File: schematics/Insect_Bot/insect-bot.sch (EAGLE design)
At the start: 26 parts, among them Q1 2N2222, U1 L4931-TO92-AMMO, U2 ARDUINO_MINI

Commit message: First completed insect bot PCB.
First revision with poured-copper ground plane.
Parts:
- added JP4, JP5: STAND-OFF, SparkFun-Electromechanical:STAND-OFF
- S2: value TILTSWITCH -> tilt
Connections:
- net GND: now also S2.1; no longer S2.2
- net N$1: now also S1.S
- net N$12: now also S2.2; no longer S2.1
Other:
- moved on the sheet: S2
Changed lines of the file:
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@@
 </variantdefs>
 <classes>
-<class number="0" name="default" width="0" drill="0">
+<class number="0" name="default" width="0.3048" drill="0.2032">
+<clearance class="0" value="0.2032"/>
+</class>
+<class number="1" name="power" width="0.4064" drill="0.2032">
+<clearance class="1" value="0.2032"/>
 </class>
 </classes>
@@
 <part name="P+7" library="SparkFun-Aesthetics" deviceset="VCC" device=""/>
 <part name="GND10" library="SparkFun-Aesthetics" deviceset="GND" device=""/>
-<part name="S2" library="jb-eagle" deviceset="TILTSWITCH" device=""/>
 <part name="GND11" library="SparkFun-Aesthetics" deviceset="GND" device=""/>
 <part name="R9" library="SparkFun-Passives" deviceset="RESISTOR" device="AXIAL-0.3" value="330"/>
 <part name="LED2" library="SparkFun-LED" deviceset="LED" device="3MM" value="red"/>
 <part name="GND12" library="SparkFun-Aesthetics" deviceset="GND" device=""/>
+<part name="S2" library="jb-eagle" deviceset="TILTSWITCH" device="" value="tilt"/>
+<part name="JP4" library="SparkFun-Electromechanical" deviceset="STAND-OFF" device=""/>
+<part name="JP5" library="SparkFun-Electromechanical" deviceset="STAND-OFF" device=""/>
 </parts>
 <sheets>
@@
 <instance part="P+7" gate="1" x="177.8" y="119.38"/>
 <instance part="GND10" gate="1" x="177.8" y="81.28"/>
-<instance part="S2" gate="G$1" x="152.4" y="81.28" rot="R270"/>
 <instance part="GND11" gate="1" x="152.4" y="71.12"/>
 <instance part="R9" gate="G$1" x="139.7" y="81.28" rot="R90"/>
 <instance part="LED2" gate="G$1" x="139.7" y="71.12"/>
 <instance part="GND12" gate="1" x="139.7" y="60.96"/>
+<instance part="S2" gate="G$1" x="152.4" y="81.28" rot="R90"/>
+<instance part="JP4" gate="G$1" x="104.14" y="-5.08"/>
+<instance part="JP5" gate="G$1" x="109.22" y="-5.08"/>
 </instances>
 <busses>
 </busses>
 <nets>
-<net name="GND" class="0">
+<net name="GND" class="1">
 <segment>
 <pinref part="JP1" gate="G$1" pin="2"/>
@@
 </segment>
 <segment>
-<pinref part="S2" gate="G$1" pin="2"/>
 <pinref part="GND11" gate="1" pin="GND"/>
 <wire x1="152.4" y1="76.2" x2="152.4" y2="73.66" width="0.1524" layer="91"/>
+<pinref part="S2" gate="G$1" pin="1"/>
 </segment>
 <segment>
@@
 </segment>
 </net>
-<net name="N$1" class="0">
+<net name="N$1" class="1">
 <segment>
 <pinref part="JP1" gate="G$1" pin="1"/>
 <pinref part="S1" gate="1" pin="P"/>
 <wire x1="-5.08" y1="22.86" x2="2.54" y2="22.86" width="0.1524" layer="91"/>
-</segment>
-</net>
-<net name="N$2" class="0">
+<pinref part="S1" gate="1" pin="S"/>
+<wire x1="10.16" y1="20.32" x2="10.16" y2="17.78" width="0.1524" layer="91"/>
+<wire x1="10.16" y1="17.78" x2="2.54" y2="17.78" width="0.1524" layer="91"/>
+<wire x1="2.54" y1="17.78" x2="2.54" y2="22.86" width="0.1524" layer="91"/>
+<junction x="2.54" y="22.86"/>
+</segment>
+</net>
+<net name="N$2" class="1">
 <segment>
 <pinref part="S1" gate="1" pin="O"/>
@@
 </segment>
 </net>
-<net name="V_IN" class="0">
+<net name="V_IN" class="1">
 <segment>
 <pinref part="D1" gate="G$1" pin="C"/>
@@
 <segment>
 <pinref part="U2" gate="G$1" pin="A0"/>
-<pinref part="S2" gate="G$1" pin="1"/>
 <wire x1="114.3" y1="88.9" x2="152.4" y2="88.9" width="0.1524" layer="91"/>
 <wire x1="152.4" y1="88.9" x2="152.4" y2="86.36" width="0.1524" layer="91"/>
-</segment>
-</net>
+<pinref part="S2" gate="G$1" pin="2"/>
+</segment>
+</net>

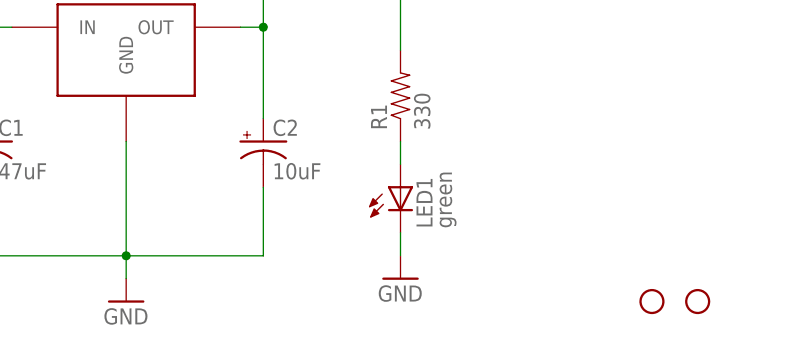
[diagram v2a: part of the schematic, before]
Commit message: Final layout for insect bot board.
Made traces a bit wider. Increased size of pad for the IR remote
receiver.
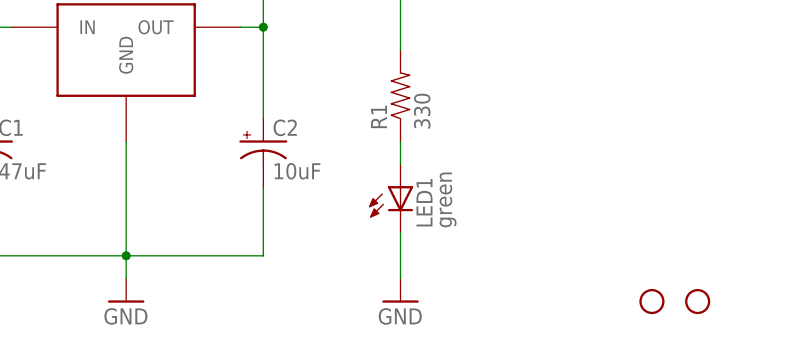
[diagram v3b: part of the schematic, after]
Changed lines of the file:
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@@
 <part name="P+6" library="SparkFun-Aesthetics" deviceset="VCC" device=""/>
 <part name="GND8" library="SparkFun-Aesthetics" deviceset="GND" device=""/>
-<part name="IRM1" library="jb-eagle" deviceset="AX-1838" device=""/>
 <part name="R6" library="SparkFun-Passives" deviceset="RESISTOR" device="AXIAL-0.3" value="47"/>
 <part name="R7" library="SparkFun-Passives" deviceset="RESISTOR" device="AXIAL-0.3" value="10k"/>
@@
 <part name="JP4" library="SparkFun-Electromechanical" deviceset="STAND-OFF" device=""/>
 <part name="JP5" library="SparkFun-Electromechanical" deviceset="STAND-OFF" device=""/>
+<part name="IRM1" library="jb-eagle" deviceset="AX-1838" device=""/>
 </parts>
 <sheets>
@@
 <instance part="GND5" gate="1" x="139.7" y="99.06"/>
 <instance part="GND6" gate="1" x="154.94" y="96.52"/>
-<instance part="GND7" gate="1" x="76.2" y="-2.54"/>
+<instance part="GND7" gate="1" x="76.2" y="-5.08"/>
 <instance part="P+5" gate="1" x="60.96" y="33.02"/>
 <instance part="JP3" gate="G$1" x="99.06" y="147.32" rot="R270"/>
 <instance part="P+6" gate="1" x="86.36" y="144.78"/>
 <instance part="GND8" gate="1" x="111.76" y="134.62"/>
-<instance part="IRM1" gate="G$1" x="35.56" y="86.36"/>
 <instance part="R6" gate="G$1" x="60.96" y="91.44"/>
 <instance part="R7" gate="G$1" x="68.58" y="86.36" rot="R90"/>
@@
 <instance part="JP4" gate="G$1" x="104.14" y="-5.08"/>
 <instance part="JP5" gate="G$1" x="109.22" y="-5.08"/>
+<instance part="IRM1" gate="G$1" x="35.56" y="86.36"/>
 </instances>
 <busses>
@@
 </segment>
 <segment>
-<pinref part="LED1" gate="G$1" pin="C"/>
-<wire x1="76.2" y1="2.54" x2="76.2" y2="0" width="0.1524" layer="91"/>
-<pinref part="GND7" gate="1" pin="GND"/>
-</segment>
-<segment>
 <pinref part="JP3" gate="G$1" pin="4"/>
 <wire x1="104.14" y1="142.24" x2="104.14" y2="139.7" width="0.1524" layer="91"/>
@@
 </segment>
 <segment>
-<pinref part="IRM1" gate="G$1" pin="GND"/>
 <wire x1="45.72" y1="81.28" x2="48.26" y2="81.28" width="0.1524" layer="91"/>
 <wire x1="48.26" y1="81.28" x2="48.26" y2="76.2" width="0.1524" layer="91"/>
@@
 <wire x1="53.34" y1="76.2" x2="53.34" y2="73.66" width="0.1524" layer="91"/>
 <junction x="53.34" y="76.2"/>
+<pinref part="IRM1" gate="G$1" pin="GND"/>
 </segment>
 <segment>
@@
 <pinref part="GND12" gate="1" pin="GND"/>
 <wire x1="139.7" y1="66.04" x2="139.7" y2="63.5" width="0.1524" layer="91"/>
+</segment>
+<segment>
+<pinref part="LED1" gate="G$1" pin="C"/>
+<pinref part="GND7" gate="1" pin="GND"/>
+<wire x1="76.2" y1="2.54" x2="76.2" y2="-2.54" width="0.1524" layer="91"/>
 </segment>
 </net>
@@
 </segment>
 <segment>
-<pinref part="IRM1" gate="G$1" pin="VCC"/>
-<pinref part="C3" gate="G$1" pin="+"/>
-<wire x1="45.72" y1="91.44" x2="53.34" y2="91.44" width="0.1524" layer="91"/>
-<wire x1="53.34" y1="91.44" x2="53.34" y2="83.82" width="0.1524" layer="91"/>
-<pinref part="R6" gate="G$1" pin="1"/>
-<wire x1="53.34" y1="91.44" x2="55.88" y2="91.44" width="0.1524" layer="91"/>
-<junction x="53.34" y="91.44"/>
-</segment>
-<segment>
 <pinref part="P+7" gate="1" pin="VCC"/>
 <pinref part="SG1" gate="G$1" pin="1"/>
@@
 <wire x1="172.72" y1="114.3" x2="177.8" y2="114.3" width="0.1524" layer="91"/>
 <junction x="177.8" y="114.3"/>
+</segment>
+<segment>
+<pinref part="C3" gate="G$1" pin="+"/>
+<wire x1="45.72" y1="91.44" x2="53.34" y2="91.44" width="0.1524" layer="91"/>
+<wire x1="53.34" y1="91.44" x2="53.34" y2="83.82" width="0.1524" layer="91"/>
+<pinref part="R6" gate="G$1" pin="1"/>
+<wire x1="53.34" y1="91.44" x2="55.88" y2="91.44" width="0.1524" layer="91"/>
+<junction x="53.34" y="91.44"/>
+<pinref part="IRM1" gate="G$1" pin="VCC"/>
 </segment>
 </net>
@@
 <net name="REMOTE" class="0">
 <segment>
-<pinref part="IRM1" gate="G$1" pin="OUT"/>
 <wire x1="45.72" y1="86.36" x2="60.96" y2="86.36" width="0.1524" layer="91"/>
 <wire x1="60.96" y1="86.36" x2="60.96" y2="81.28" width="0.1524" layer="91"/>
 <pinref part="R7" gate="G$1" pin="1"/>
 <wire x1="60.96" y1="81.28" x2="68.58" y2="81.28" width="0.1524" layer="91"/>
-</segment>
-</net>
+<pinref part="IRM1" gate="G$1" pin="OUT"/>
+</segment>
+</net>
